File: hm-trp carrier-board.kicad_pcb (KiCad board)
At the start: 2 copper layers, 16.1 x 29.3 mm, 3 parts, among them J1 Conn_01x06, J2 Conn_Coaxial

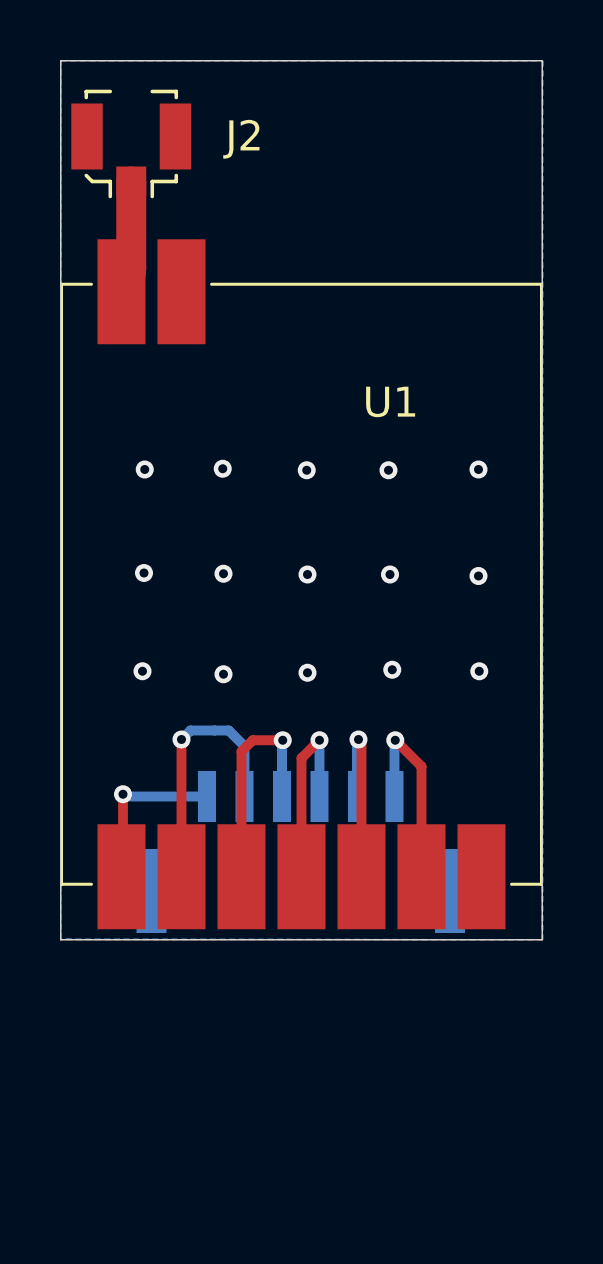
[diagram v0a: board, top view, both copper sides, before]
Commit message: Version 2.0: GH1.25 Connector is moved from the bottom side to the top side and PCB is also panalised
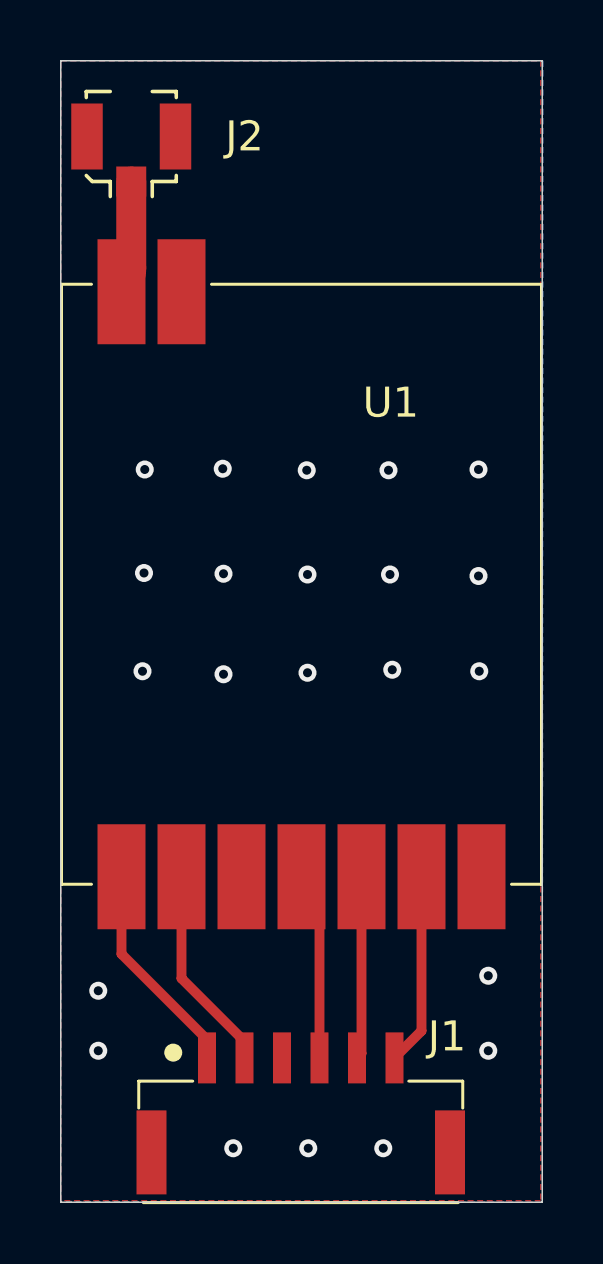
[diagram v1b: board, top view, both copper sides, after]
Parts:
- J1: moved to F.Cu
- moved J1 8.71 mm to (8.00, 34.8), turned to 0 degrees
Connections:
- J1 pad 1: /Enable -> /Vcc
- J1 pad 2: /Config -> /DTX
- J1 pad 3: /DRX -> GND
- J1 pad 4: GND -> /DRX
- J1 pad 5: /DTX -> /Config
- J1 pad 6: /Vcc -> /Enable
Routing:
- net GND: track 7.59 -> 0.00 mm, vias 16 -> 22
- net /DTX: track 8.69 -> 6.91 mm, vias 1 -> 0
- net /Vcc: track 5.60 -> 7.22 mm, vias 1 -> 0
- net /Config: track 6.54 -> 6.10 mm, vias 1 -> 0
- net /DRX: track 6.67 -> 6.29 mm, vias 1 -> 0
- net /Enable: track 6.80 -> 6.41 mm, vias 1 -> 0
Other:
- board size 16.1 x 29.3 mm -> 16.1 x 38 mm
